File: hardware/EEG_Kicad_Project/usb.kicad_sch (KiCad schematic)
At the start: 0 parts

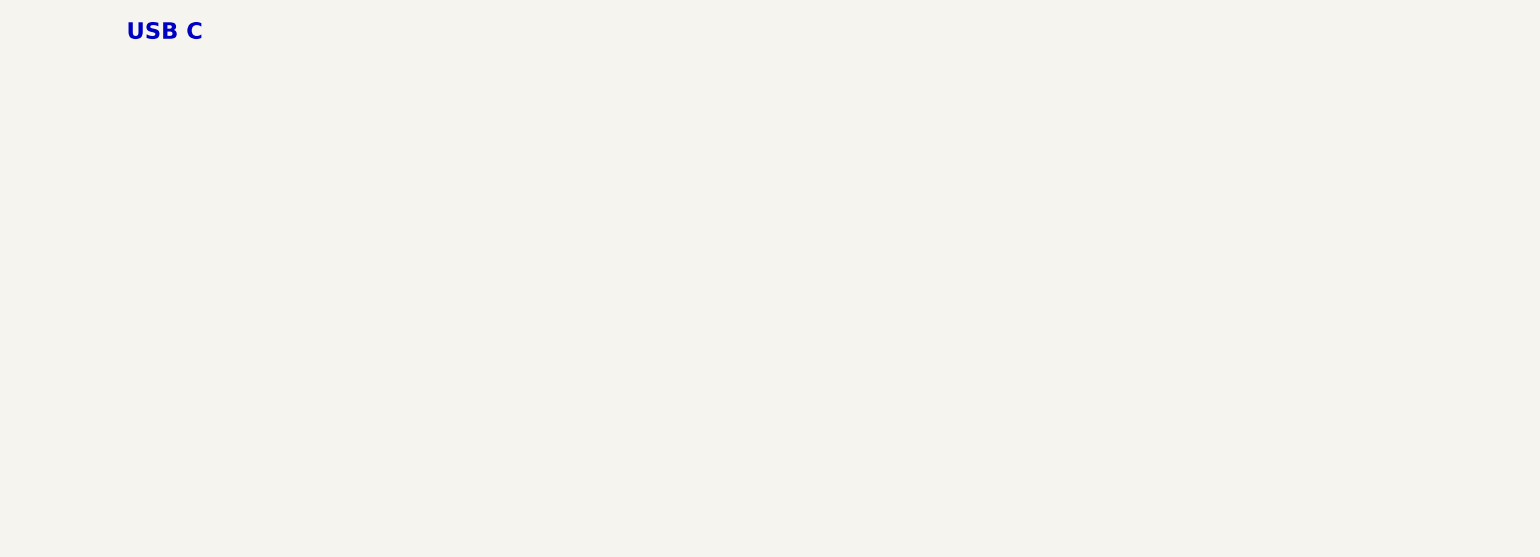
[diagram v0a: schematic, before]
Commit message: Add USB galvanic isolation barrier for patient safety
Adds a USB-C receptacle -> ESD protection -> ADuM3160 isolator ->
isolated TMU3-0511 DC-DC chain, separating the STM32/ADS1299/analog
supply (now fully isolated) from the non-isolated USB-connector side.
Closes the previously-floating USB_OTG_FS_DP/DM pins on the STM32,
adds CC1/CC2 pulldowns and VBUS decoupling on the new receptacle, and
fixes ADuM3160 VBUS2 tie per datasheet. Verified via kicad-happy: no
ERC regressions, isolation barrier confirmed intact (no net bridges
GND_PRI/+5V_PRI with the isolated GNDA/+5V/+3V3 domain).

Co-Authored-By: Claude Sonnet 5 <noreply@anthropic.com>
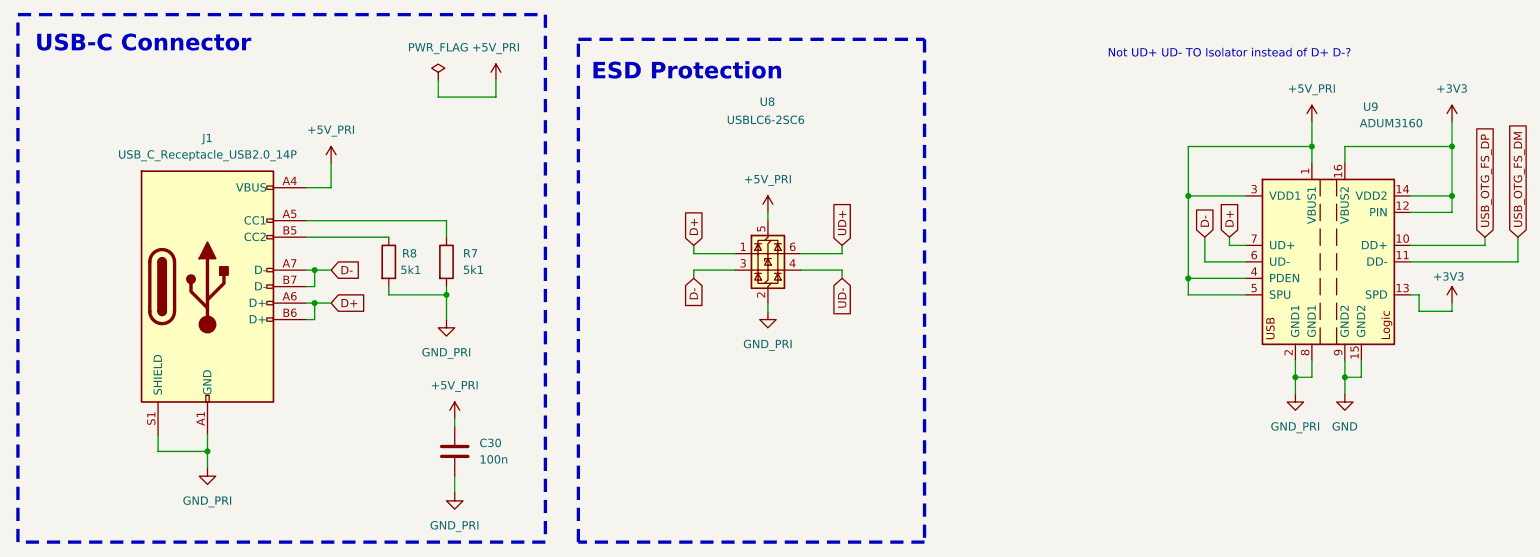
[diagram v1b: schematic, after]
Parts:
- added C30: 100n, Capacitor_SMD:C_0402_1005Metric, symbol Device:C
- added J1: USB_C_Receptacle_USB2.0_14P, symbol Connector:USB_C_Receptacle_USB2.0_14P
- added R7, R8: 5k1, Resistor_SMD:R_0402_1005Metric_Pad0.72x0.64mm_HandSolder, symbol Device:R
- added U8: USBLC6-2SC6, Package_TO_SOT_SMD:SOT-23-6, symbol Power_Protection:USBLC6-2SC6
- added U9: ADUM3160, Package_SO:SOIC-16W_7.5x10.3mm_P1.27mm, symbol Interface_USB:ADUM3160
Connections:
- new net: J1.B5 (CC2), R8.1
- new net: J1.A5 (CC1), R7.1
- new net +3V3: U9.12 (PIN), U9.13 (SPD), U9.14 (VDD2), U9.16 (VBUS2)
- new net +5V_PRI: C30.1, J1.A4 (VBUS), J1.A9 (VBUS), J1.B4 (VBUS), J1.B9 (VBUS), U8.5 (VBUS), U9.1 (VBUS1), U9.3 (VDD1), U9.4 (PDEN), U9.5 (SPU)
- new net D+: J1.A6 (D+), J1.B6 (D+), U8.1 (I/O1), U9.7 (UD+)
- new net D-: J1.A7 (D-), J1.B7 (D-), U8.3 (I/O2), U9.6 (UD-)
- new net GND: U9.15 (GND2), U9.9 (GND2)
- new net GND_PRI: C30.2, J1.A1 (GND), J1.A12 (GND), J1.B1 (GND), J1.B12 (GND), J1.S1 (SHIELD), R7.2, R8.2, U8.2 (GND), U9.2 (GND1), U9.8 (GND1)
- new net UD+: U8.6 (I/O1)
- new net UD-: U8.4 (I/O2)
- new net USB_OTG_FS_DM: U9.11 (DD-)
- new net USB_OTG_FS_DP: U9.10 (DD+)
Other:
- note added: "ESD Protection"
- note added: "Not UD+ UD- TO Isolator instead of D+ D-?"
- note added: "USB-C Connector"
- note removed: "USB C"
